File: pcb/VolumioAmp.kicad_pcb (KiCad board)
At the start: 2 copper layers, 136 x 71.2 mm, 50 parts, among them IC1 PCM2706, J2 Barrel_Jack, Q1 DMP3013SFV-7, U1 TPD4EUSB30, U2 TPD4EUSB30, U3 MagJack-A70-112-331N126, U4 AP64501SP-13, U6 MA12040PXUMA1, U7 74LVC1G07SE-7, U8 FSUSB42MUX

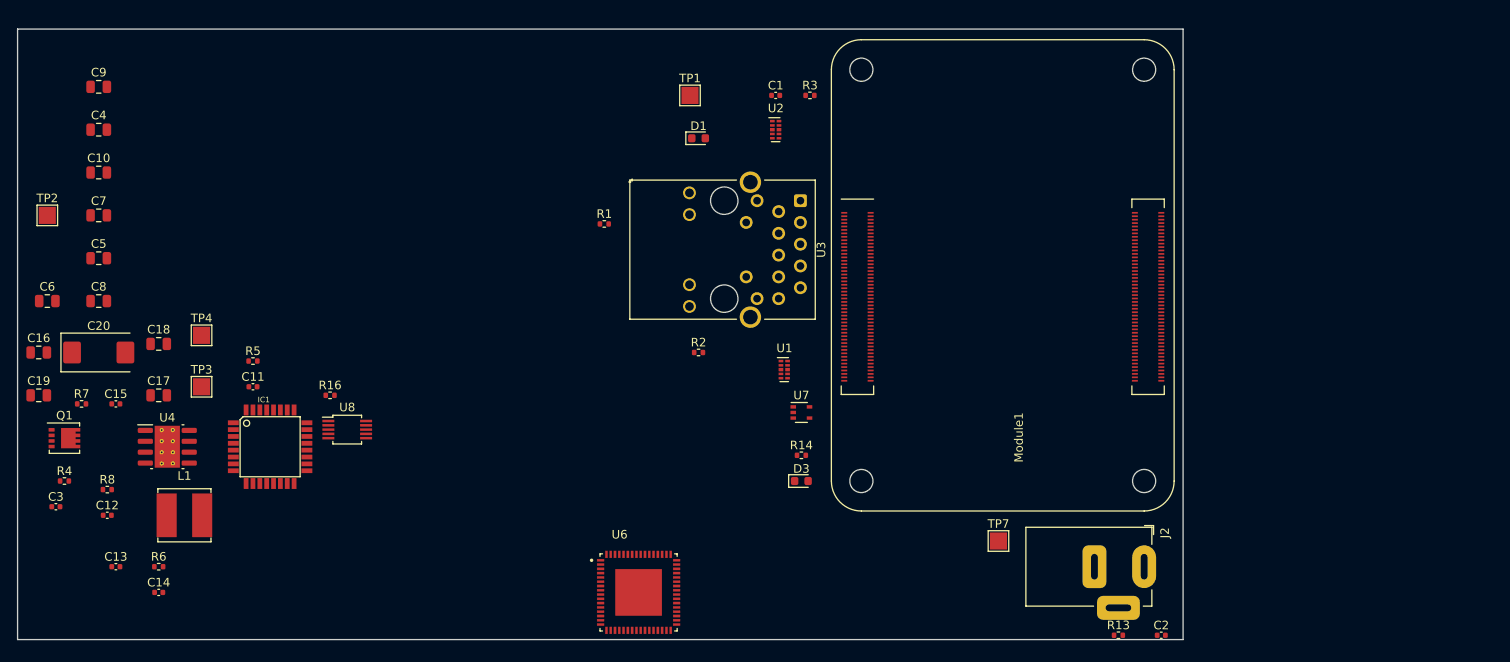
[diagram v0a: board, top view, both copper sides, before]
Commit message: - USB sound wired
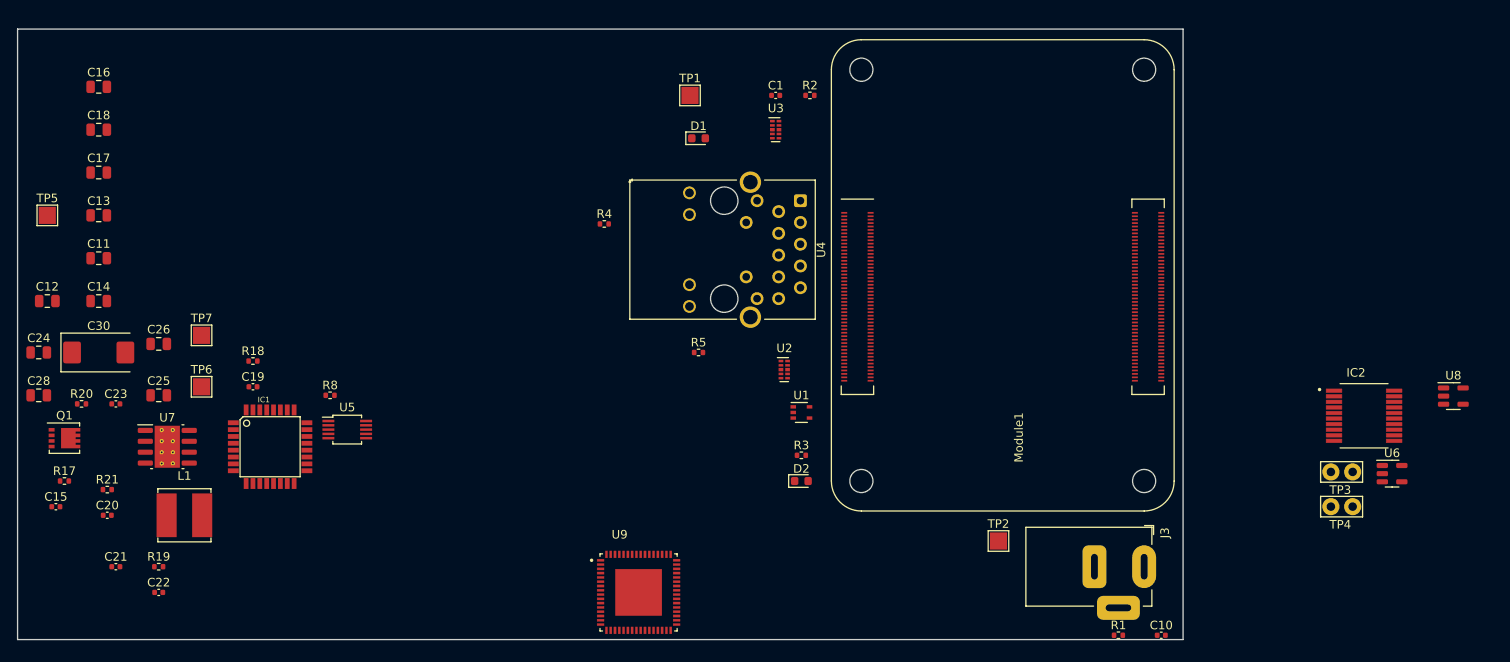
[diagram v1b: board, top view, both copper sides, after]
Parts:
- added IC2: WM8804GEDS_V, Footprints:SOP65P780X200-20N, F.Cu at (190.7, 69.4)
- added TP3: TestPoint, TestPoint:TestPoint_Bridge_Pitch2.54mm_Drill1.0mm, F.Cu at (186.8, 75.9)
- added TP4: TestPoint, TestPoint:TestPoint_Bridge_Pitch2.54mm_Drill1.0mm, F.Cu at (186.8, 80.0)
- added U6: 24AA02-OT, Package_TO_SOT_SMD:SOT-23-5, F.Cu at (193.9, 76.1)
- added U8: LT1761-3.3, Package_TO_SOT_SMD:TSOT-23-5, F.Cu at (201.1, 67.1)
- renumbered C2 to C10, C5 to C11, C6 to C12, C7 to C13, C8 to C14, C3 to C15, C9 to C16, C10 to C17, C4 to C18, C11 to C19, C12 to C20, C13 to C21, C14 to C22, C15 to C23, C16 to C24, C17 to C25, C18 to C26, C19 to C28, C20 to C30, D3 to D2, J2 to J3, R13 to R1, R4 to R17, R5 to R18, R6 to R19, R3 to R2, R7 to R20, R8 to R21, R14 to R3, R1 to R4, R2 to R5, R16 to R8, TP7 to TP2, TP2 to TP5, TP3 to TP6, TP4 to TP7, U7 to U1, U1 to U2, U2 to U3, U3 to U4, U8 to U5, U4 to U7, U6 to U9
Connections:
- IC1 pad 1: unconnected-(IC1-PGND-Pad1) -> GND
- IC1 pad 10: unconnected-(IC1-TEST-Pad10) -> /USB_Sound/+3.3v
- IC1 pad 12: unconnected-(IC1-XTI-Pad12) -> Net-(IC1-XTI)
- IC1 pad 13: unconnected-(IC1-XTO-Pad13) -> Net-(IC1-XTO)
- IC1 pad 14: unconnected-(IC1-CK-Pad14) -> /USB_Sound/SCL
- IC1 pad 15: unconnected-(IC1-DT-Pad15) -> /USB_Sound/SDA
- IC1 pad 16: unconnected-(IC1-PSEL-Pad16) -> GND
- IC1 pad 2: unconnected-(IC1-VCCP-Pad2) -> /USB_Sound/+3.3v
- IC1 pad 20: unconnected-(IC1-DGND-Pad20) -> GND
- IC1 pad 21: unconnected-(IC1-VDD-Pad21) -> /USB_Sound/+3.3v
- IC1 pad 24: unconnected-(IC1-VBUS-Pad24) -> /USB_Sound/+3.3v
- IC1 pad 25: unconnected-(IC1-ZGND-Pad25) -> GND
- IC1 pad 26: unconnected-(IC1-AGNDL-Pad26) -> GND
- IC1 pad 27: unconnected-(IC1-VCCL-Pad27) -> /USB_Sound/+3.3v
- IC1 pad 28: unconnected-(IC1-VOUTL-Pad28) -> Net-(IC1-VOUTL)
- IC1 pad 29: unconnected-(IC1-VOUTR-Pad29) -> Net-(IC1-VOUTR)
- IC1 pad 3: unconnected-(IC1-HOST-Pad3) -> Net-(IC1-HOST)
- IC1 pad 30: unconnected-(IC1-VCCR-Pad30) -> /USB_Sound/+3.3v
- IC1 pad 31: unconnected-(IC1-AGNDR-Pad31) -> GND
- IC1 pad 32: unconnected-(IC1-VCOM-Pad32) -> Net-(IC1-VCOM)
- IC1 pad 9: unconnected-(IC1-FSEL-Pad9) -> GND
- U5 pad 1: unconnected-(U8-VCC-Pad1) -> /USB_Sound/+3.3v

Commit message: WM8804 via i2c
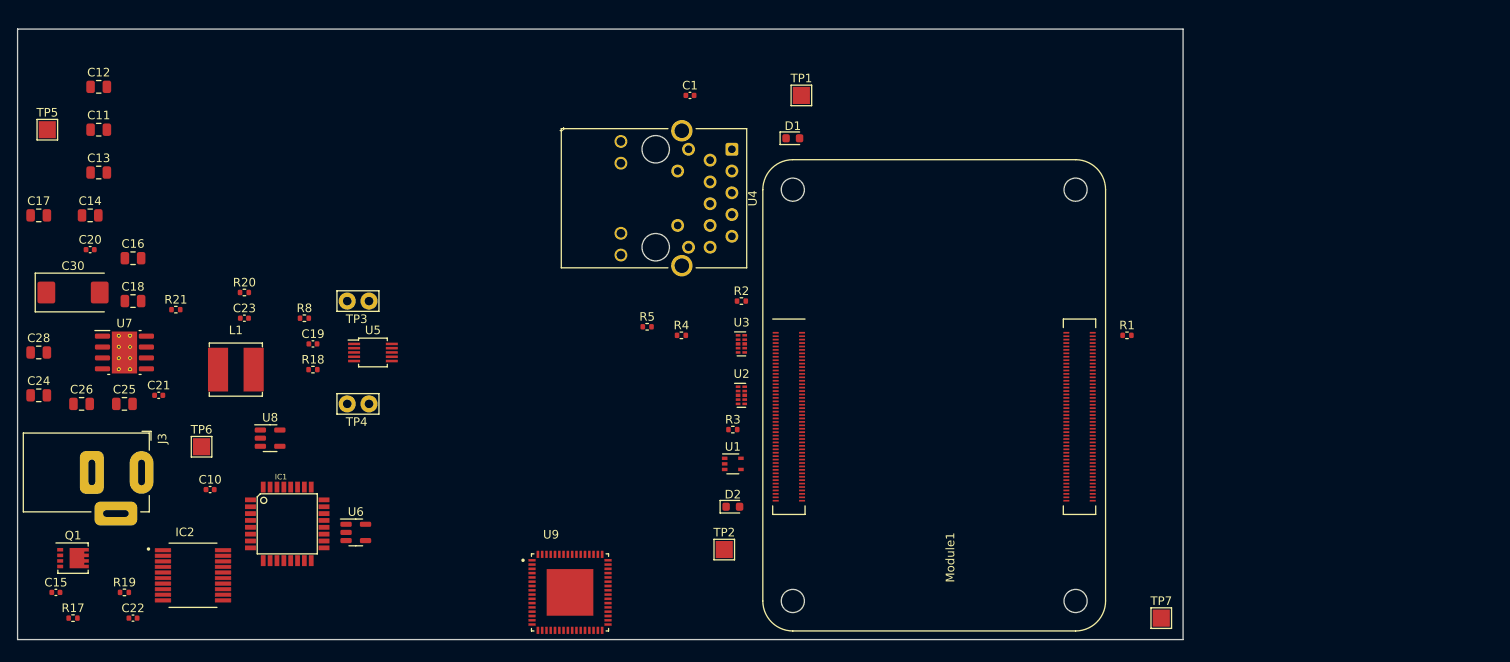
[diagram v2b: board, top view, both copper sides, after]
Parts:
- moved U8 138.2 mm to (63.0, 72.0)
- moved IC2 137.9 mm to (54.0, 88.0)
- moved U6 121.1 mm to (73.0, 83.0)
- moved J3 117.5 mm to (48.0, 76.0)
- moved TP7 116.8 mm to (167.0, 93.0)
- moved TP3 116.5 mm to (72.0, 56.0)
- moved TP4 115.4 mm to (72.0, 68.0)
- moved C10 112.3 mm to (56.0, 78.0)
- moved R1 35.0 mm to (163.0, 60.0)
- moved TP2 32.0 mm to (116.0, 85.0)
- moved C20 31.1 mm to (42.0, 50.0)
- moved C12 25.7 mm to (43.0, 31.0)
- moved U3 25.3 mm to (118.0, 61.0)
- moved R2 25.3 mm to (118.0, 56.0)
- moved R20 23.0 mm to (60.0, 55.0)
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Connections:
- C23 pad 1: /Power/+5v -> /CM4_Ethernet/+5v
- C24 pad 1: /Power/+5v -> /CM4_Ethernet/+5v
- C25 pad 1: /Power/+5v -> /CM4_Ethernet/+5v
- C26 pad 1: /Power/+5v -> /CM4_Ethernet/+5v
- C28 pad 1: /Power/+5v -> /CM4_Ethernet/+5v
- C30 pad 1: /Power/+5v -> /CM4_Ethernet/+5v
- IC1 pad 10: /USB_Sound/+3.3v -> /Power/+3.3v
- IC1 pad 14: /USB_Sound/SCL -> /Amplifier/SCL
- IC1 pad 15: /USB_Sound/SDA -> /Amplifier/SDA
- IC1 pad 17: /USB_Sound/DOUT -> /Amplifier/DIN
- IC1 pad 18: unconnected-(IC1-FUNC2-Pad18) -> /Amplifier/MCK
- IC1 pad 19: /USB_Sound/BCK -> /Amplifier/BCK
- IC1 pad 2: /USB_Sound/+3.3v -> /Power/+3.3v
- IC1 pad 21: /USB_Sound/+3.3v -> /Power/+3.3v
- IC1 pad 24: /USB_Sound/+3.3v -> /Power/+3.3v
- IC1 pad 27: /USB_Sound/+3.3v -> /Power/+3.3v
- IC1 pad 30: /USB_Sound/+3.3v -> /Power/+3.3v
- IC1 pad 5: /USB_Sound/LRCK -> /Amplifier/LRCK
- IC2 pad 10: unconnected-(IC2-XOP-Pad10) -> Net-(IC2-XOP)
- IC2 pad 11: unconnected-(IC2-XIN-Pad11) -> Net-(IC2-XIN)
- IC2 pad 13: unconnected-(IC2-DIN-Pad13) -> /Amplifier/DIN
- IC2 pad 14: unconnected-(IC2-BCLK-Pad14) -> /Amplifier/BCK
- IC2 pad 15: unconnected-(IC2-LRCLK-Pad15) -> /Amplifier/LRCK
- IC2 pad 16: unconnected-(IC2-MCLK-Pad16) -> /Amplifier/MCK
- IC2 pad 18: unconnected-(IC2-DGND-Pad18) -> GND
- IC2 pad 19: unconnected-(IC2-DVDD-Pad19) -> /Power/+3.3v
- IC2 pad 7: unconnected-(IC2-PVDD-Pad7) -> /Power/+3.3v
- IC2 pad 8: unconnected-(IC2-PGND-Pad8) -> GND
- L1 pad 2: /Power/+5v -> /CM4_Ethernet/+5v
- Module1 pad 80: /CM4_Ethernet/SCL0 -> /Amplifier/SCL
- Module1 pad 82: /CM4_Ethernet/SDA0 -> /Amplifier/SDA
- R20 pad 1: /Power/+5v -> /CM4_Ethernet/+5v
- TP6 pad 1: /Power/+5v -> /CM4_Ethernet/+5v
- U5 pad 1: /USB_Sound/+3.3v -> /Power/+3.3v
- U6 pad 1: /USB_Sound/SCL -> /Amplifier/SCL
- U6 pad 3: /USB_Sound/SDA -> /Amplifier/SDA
- U6 pad 4: /USB_Sound/+3.3v -> /Power/+3.3v
- U8 pad 1: /Power/+5v -> /CM4_Ethernet/+5v
- U8 pad 3: /Power/+5v -> /CM4_Ethernet/+5v

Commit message: - work in progress
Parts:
- added TP8: TestPoint, TestPoint:TestPoint_Bridge_Pitch2.54mm_Drill1.0mm, F.Cu at (64.9, 44.1)
- added TP9: TestPoint, TestPoint:TestPoint_Bridge_Pitch2.54mm_Drill1.0mm, F.Cu at (64.9, 48.2)
- moved IC2 54.5 mm to (68.8, 35.6)
- moved U6 10.9 mm to (81.2, 90.3)
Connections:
- net /Amplifier/BCK renamed /Amplifier/I2S.BCK
- net /Amplifier/DIN renamed /Amplifier/I2S.D
- net /Amplifier/LRCK renamed /Amplifier/I2S.LRCK
- net /Amplifier/MCK renamed /Amplifier/I2S.MCK
- IC1 pad 10: /Power/+3.3v -> /I2STest/+3.3v
- IC1 pad 2: /Power/+3.3v -> /I2STest/+3.3v
- IC1 pad 21: /Power/+3.3v -> /I2STest/+3.3v
- IC1 pad 24: /Power/+3.3v -> /I2STest/+3.3v
- IC1 pad 27: /Power/+3.3v -> /I2STest/+3.3v
- IC1 pad 30: /Power/+3.3v -> /I2STest/+3.3v
- IC2 pad 1: unconnected-(IC2-SCLK-Pad1) -> /Amplifier/SCL
- IC2 pad 17: unconnected-(IC2-TX0-Pad17) -> Net-(IC2-TX0)
- IC2 pad 19: /Power/+3.3v -> /I2STest/+3.3v
- IC2 pad 2: unconnected-(IC2-GPO0/SWIFMODE-Pad2) -> GND
- IC2 pad 3: unconnected-(IC2-SDIN/HWMODE-Pad3) -> /Amplifier/SDA
- IC2 pad 6: unconnected-(IC2-RESETB-Pad6) -> /I2STest/+3.3v
- IC2 pad 7: /Power/+3.3v -> /I2STest/+3.3v
- U5 pad 1: /Power/+3.3v -> /I2STest/+3.3v
- U6 pad 4: /Power/+3.3v -> /I2STest/+3.3v
- U8 pad 5: /Power/+3.3v -> /I2STest/+3.3v

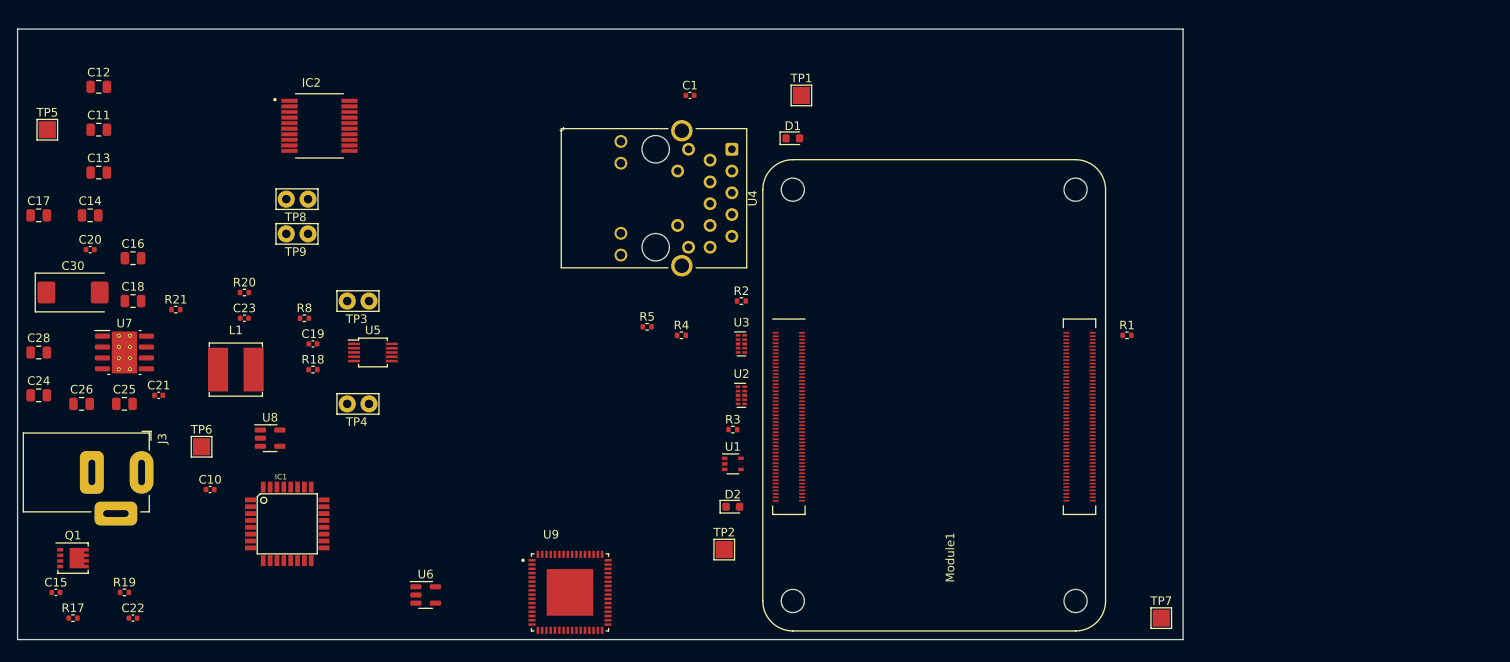
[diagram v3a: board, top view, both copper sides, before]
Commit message: - voor aanpassing design rules jclpcb
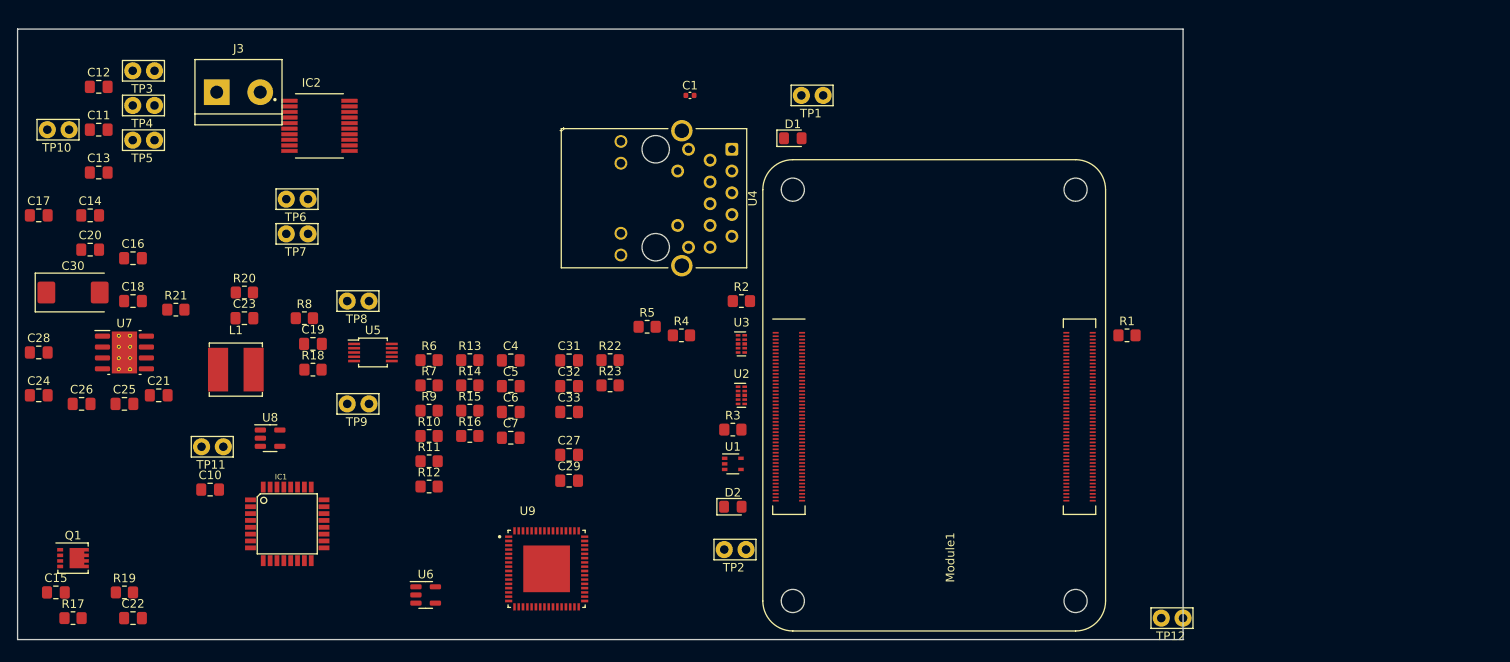
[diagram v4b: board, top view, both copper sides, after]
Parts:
- added C27: 10n, Capacitor_SMD:C_0805_2012Metric_Pad1.18x1.45mm_HandSolder, F.Cu at (97.9, 74.0)
- added C29: 1u, Capacitor_SMD:C_0805_2012Metric_Pad1.18x1.45mm_HandSolder, F.Cu at (97.9, 77.0)
- added C31: 22n, Capacitor_SMD:C_0805_2012Metric_Pad1.18x1.45mm_HandSolder, F.Cu at (97.9, 62.9)
- added C32: 22n, Capacitor_SMD:C_0805_2012Metric_Pad1.18x1.45mm_HandSolder, F.Cu at (97.9, 65.9)
- added C33: C, Capacitor_SMD:C_0805_2012Metric_Pad1.18x1.45mm_HandSolder, F.Cu at (97.9, 68.9)
- added C4: 22n, Capacitor_SMD:C_0805_2012Metric_Pad1.18x1.45mm_HandSolder, F.Cu at (91.1, 62.9)
- added C5: 22n, Capacitor_SMD:C_0805_2012Metric_Pad1.18x1.45mm_HandSolder, F.Cu at (91.1, 65.9)
- added C6: 22n, Capacitor_SMD:C_0805_2012Metric_Pad1.18x1.45mm_HandSolder, F.Cu at (91.1, 68.9)
- added C7: 22n, Capacitor_SMD:C_0805_2012Metric_Pad1.18x1.45mm_HandSolder, F.Cu at (91.1, 72.0)
- added R10: 13R, Resistor_SMD:R_0805_2012Metric_Pad1.20x1.40mm_HandSolder, F.Cu at (81.6, 71.7)
- added R11: 1k5, Resistor_SMD:R_0805_2012Metric_Pad1.20x1.40mm_HandSolder, F.Cu at (81.6, 74.7)
- added R12: 13R, Resistor_SMD:R_0805_2012Metric_Pad1.20x1.40mm_HandSolder, F.Cu at (81.6, 77.6)
- added R13: 3k3, Resistor_SMD:R_0805_2012Metric_Pad1.20x1.40mm_HandSolder, F.Cu at (86.3, 62.9)
- added R14: 3k3, Resistor_SMD:R_0805_2012Metric_Pad1.20x1.40mm_HandSolder, F.Cu at (86.3, 65.8)
- added R15: 3k3, Resistor_SMD:R_0805_2012Metric_Pad1.20x1.40mm_HandSolder, F.Cu at (86.3, 68.8)
- added R16: 3k3, Resistor_SMD:R_0805_2012Metric_Pad1.20x1.40mm_HandSolder, F.Cu at (86.3, 71.7)
- added R22: R, Resistor_SMD:R_0805_2012Metric_Pad1.20x1.40mm_HandSolder, F.Cu at (102.7, 62.9)
- added R23: R, Resistor_SMD:R_0805_2012Metric_Pad1.20x1.40mm_HandSolder, F.Cu at (102.7, 65.8)
- added R6: 1k, Resistor_SMD:R_0805_2012Metric_Pad1.20x1.40mm_HandSolder, F.Cu at (81.6, 62.9)
- added R7: 1M, Resistor_SMD:R_0805_2012Metric_Pad1.20x1.40mm_HandSolder, F.Cu at (81.6, 65.8)
- added R9: 1k5, Resistor_SMD:R_0805_2012Metric_Pad1.20x1.40mm_HandSolder, F.Cu at (81.6, 68.8)
- added TP3: Host, TestPoint:TestPoint_Bridge_Pitch2.54mm_Drill1.0mm, F.Cu at (47.0, 29.1)
- added TP4: TestPoint, TestPoint:TestPoint_Bridge_Pitch2.54mm_Drill1.0mm, F.Cu at (47.0, 33.2)
- added TP5: TestPoint, TestPoint:TestPoint_Bridge_Pitch2.54mm_Drill1.0mm, F.Cu at (47.0, 37.2)
- C10, C15, C19, C20, C21, C22, C23: footprint Capacitor_SMD:C_0402_1005Metric -> Capacitor_SMD:C_0805_2012Metric_Pad1.18x1.45mm_HandSolder
- C11, C12, C13, C14, C16, C17, C18, C24, C25, C26, C28: footprint Capacitor_SMD:C_0805_2012Metric -> Capacitor_SMD:C_0805_2012Metric_Pad1.18x1.45mm_HandSolder
- D1, D2: footprint LED_SMD:LED_0603_1608Metric -> LED_SMD:LED_0805_2012Metric_Pad1.15x1.40mm_HandSolder
- J3: value Barrel_Jack -> 24v Input; footprint CM4IO:BarrelJack_Horizontal -> TerminalBlock:TerminalBlock_bornier-2_P5.08mm
- R1, R17, R18, R19, R2, R20, R21, R3, R4, R5, R8: footprint Resistor_SMD:R_0402_1005Metric -> Resistor_SMD:R_0805_2012Metric_Pad1.20x1.40mm_HandSolder
- TP1, TP2: footprint TestPoint:TestPoint_Pad_2.0x2.0mm -> TestPoint:TestPoint_Bridge_Pitch2.54mm_Drill1.0mm
- TP10: renamed from TP5; footprint TestPoint:TestPoint_Pad_2.0x2.0mm -> TestPoint:TestPoint_Bridge_Pitch2.54mm_Drill1.0mm
- TP11: renamed from TP6; footprint TestPoint:TestPoint_Pad_2.0x2.0mm -> TestPoint:TestPoint_Bridge_Pitch2.54mm_Drill1.0mm
- TP12: renamed from TP7; footprint TestPoint:TestPoint_Pad_2.0x2.0mm -> TestPoint:TestPoint_Bridge_Pitch2.54mm_Drill1.0mm
- U9: footprint Libraries:QFN50P900X900X90-65N -> Footprints:QFN50P900X900X90-65N
- moved J3 45.2 mm to (56.8, 31.6)
- moved U9 3.88 mm to (95.3, 87.2)
- renumbered TP8 to TP6, TP9 to TP7, TP3 to TP8, TP4 to TP9
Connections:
- net /CM4_HighSpeed/USB2_P renamed /USB_Sound/USB_P
- C10 pad 1: Net-(Q1-D) -> Net-(J3-Pin_2)
- IC1 pad 17: /Amplifier/I2S.D -> Net-(IC1-DOUT)
- IC1 pad 18: /Amplifier/I2S.MCK -> Net-(IC1-FUNC2)
- IC1 pad 19: /Amplifier/I2S.BCK -> Net-(IC1-FUNC1)
- IC1 pad 5: /Amplifier/I2S.LRCK -> Net-(IC1-FUNC0)
- J3 pad 1: Net-(Q1-D) -> GND
- J3 pad 2: GND -> Net-(J3-Pin_2)
- Q1 pad 5: Net-(Q1-D) -> Net-(J3-Pin_2)
